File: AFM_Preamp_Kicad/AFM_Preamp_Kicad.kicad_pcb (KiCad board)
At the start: 2 copper layers, 19 parts, among them P1 DIN_5, U1 TL071, U2 TL071, U3 TL071, U4 TUNING_FORK

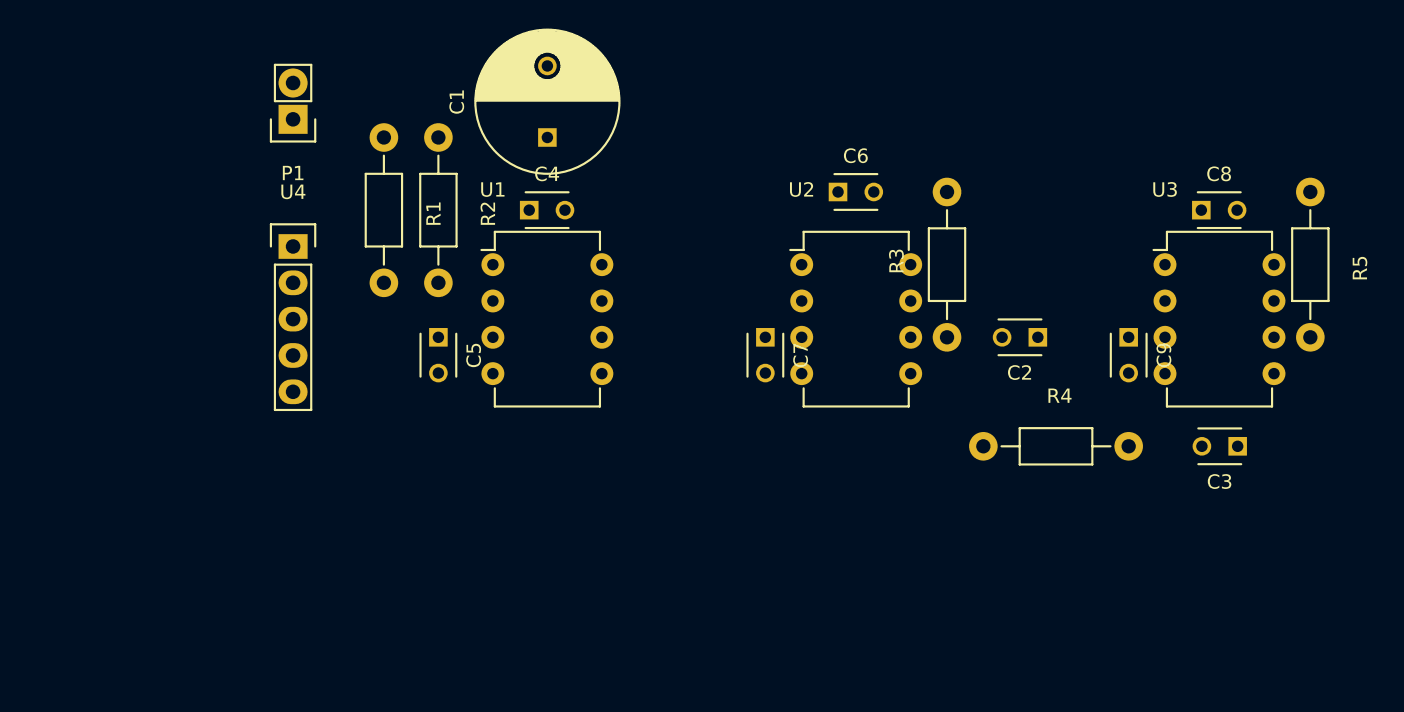
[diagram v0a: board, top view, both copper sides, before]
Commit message: add preamp schematic
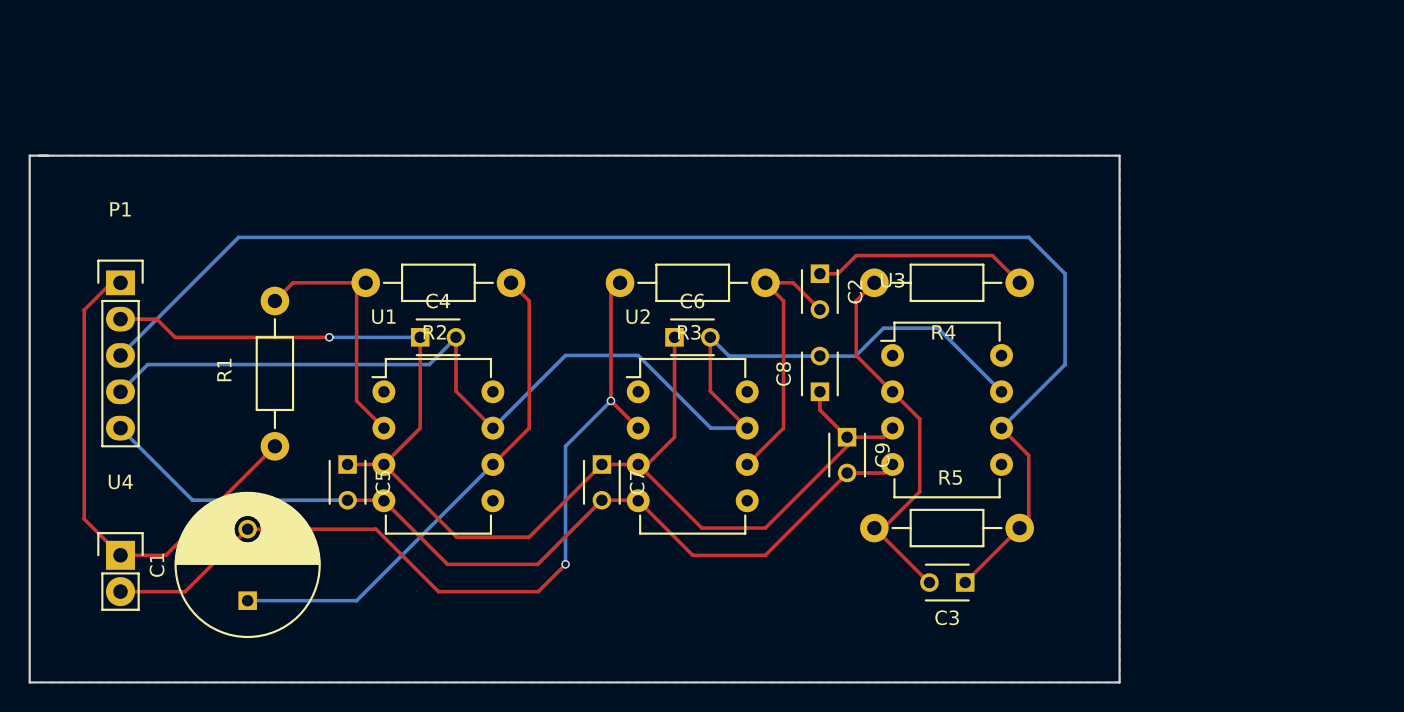
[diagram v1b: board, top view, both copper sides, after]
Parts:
- moved C1 38.6 mm to (118.7, 132.7)
- moved R5 38.5 mm to (162.6, 127.6), turned to 0 degrees
- moved U4 32.8 mm to (109.9, 129.5), turned to 0 degrees
- moved C8 29.5 mm to (158.8, 118.1), turned to 90 degrees
- moved R1 22.9 mm to (120.7, 121.9), turned to 90 degrees
- moved C3 21.3 mm to (168.9, 131.4)
- moved C9 20.9 mm to (160.7, 121.3)
- moved U3 20.1 mm to (163.8, 115.6)
- moved C2 15.9 mm to (158.8, 109.9), turned to 270 degrees
- moved C6 15.3 mm to (148.6, 114.3)
- moved C7 14.5 mm to (143.5, 123.2)
- moved U2 14.5 mm to (146.1, 118.1)
- moved R3 13.3 mm to (154.9, 110.5), turned to 180 degrees
- moved P1 12.3 mm to (109.9, 110.5)
- moved R4 11.7 mm to (172.7, 110.5), turned to 180 degrees
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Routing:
- net Amp: track 0.00 -> 96.6 mm
- net Earth: track 0.00 -> 93.1 mm, vias 0 -> 1
- net +15V: track 0.00 -> 85.5 mm
- net -15V: track 0.00 -> 64.0 mm
- net Net-(C1-Pad2): track 0.00 -> 59.5 mm, vias 0 -> 2
- net FrequencyRef: track 0.00 -> 35.5 mm
- net Net-(C1-Pad1): track 0.00 -> 35.4 mm
- net Net-(C3-Pad2): track 0.00 -> 26.6 mm
- net Net-(C2-Pad2): track 0.00 -> 18.9 mm
- net Net-(R1-Pad2): track 0.00 -> 18.1 mm
- net Net-(C2-Pad1): track 0.00 -> 15.3 mm
- added copper zone on B.Cu, net Earth
- added copper zone on F.Cu, net Earth
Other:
- board outline added: 76.2 x 36.8 mm
- net class Default: trace_width 0.25 -> 0.4
